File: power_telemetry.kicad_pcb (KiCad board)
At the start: 2 copper layers, 86.5 x 70 mm, 44 parts, among them J1 CONN_01X02, J10 CONN_01X04, J11 CONN_01X04, J12 GS2, J2 Screw_Terminal_1x02, J3 Screw_Terminal_1x02, J4 CONN_01X03, J5 CONN_01X02, J6 CONN_01X03, J7 CONN_01X02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

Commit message: more pcb latyout
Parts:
- moved R14 10.6 mm to (122.5, 94.2), turned to 0 degrees
- moved C8 8.33 mm to (132.9, 87.3)
- moved C2 8.33 mm to (130.3, 87.3)
- moved R10 8.19 mm to (155.8, 89.9)
- moved R11 8.19 mm to (151.1, 91.9)
- moved R13 8.19 mm to (146.2, 89.9)
- moved R5 8.14 mm to (125.2, 100.5)
- moved R12 7.24 mm to (146.2, 82.8)
- moved R9 7.24 mm to (151.0, 80.8)
- moved R8 7.24 mm to (155.7, 82.8)
- moved U2 5.36 mm to (137.9, 86.3), turned to 0 degrees
- moved R4 4.91 mm to (121.9, 100.5)
- moved J12 4.45 mm to (128.0, 94.2), turned to 270 degrees
- moved J1 3.25 mm to (147.4, 100.0)
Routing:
- net /SDA: track 23.5 -> 59.3 mm
- net +12V: track 184.7 -> 153.0 mm
- net Net-(J10-Pad4): track 39.0 -> 17.2 mm
- net /SCL: track 48.3 -> 31.6 mm
- net Net-(J11-Pad4): track 24.0 -> 10.0 mm
- net Net-(R11-Pad1): track 13.9 -> 27.1 mm
- net VCC: track 99.5 -> 90.9 mm
- net Net-(R12-Pad1): track 13.3 -> 18.2 mm
- net Net-(J12-Pad2): track 0.00 -> 2.98 mm
- net GND: track 27.0 -> 25.4 mm, vias 13 -> 12

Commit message: some changes
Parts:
- moved R14 14.7 mm to (136.7, 98.1)
- moved J12 13.7 mm to (141.5, 96.6), turned to 180 degrees
- moved D2 6.68 mm to (154.6, 79.9)
- moved C1 6.40 mm to (112.0, 96.2)
- moved C7 6.40 mm to (112.0, 93.4)
- moved R3 6.40 mm to (97.0, 100.8)
- moved R6 6.40 mm to (105.4, 104.8)
- moved R7 6.40 mm to (105.4, 96.8)
- moved U1 6.40 mm to (116.7, 100.4)
- moved C3 6.40 mm to (108.6, 100.8)
- moved R5 6.33 mm to (129.7, 105.0)
- moved R4 6.33 mm to (126.3, 105.0)
- moved F6 4.80 mm to (83.3, 93.6)
- moved C2 4.75 mm to (130.3, 92.1)
- moved C8 4.75 mm to (132.9, 92.1)
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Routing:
- net Net-(J10-Pad3): track 2.70 -> 38.7 mm
- net Net-(J11-Pad3): track 2.75 -> 34.9 mm
- net VCC: track 90.9 -> 120.0 mm
- net Net-(J10-Pad4): track 17.2 -> 41.2 mm, vias 0 -> 2
- net Net-(J11-Pad4): track 10.0 -> 28.1 mm
- net /SCL: track 31.6 -> 49.3 mm, vias 0 -> 2
- net Net-(F6-Pad1): track 44.9 -> 31.3 mm
- net Net-(J12-Pad2): track 2.98 -> 12.8 mm
- net Net-(F6-Pad2): track 5.86 -> 10.7 mm
- net +12V: track 153.0 -> 157.4 mm
- net /SDA: track 59.3 -> 57.9 mm
- net GND: track 25.4 -> 26.8 mm, vias 12 -> 13
- net (no net): vias 0 -> 1
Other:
- board size 86.5 x 70 mm -> 86.5 x 62 mm

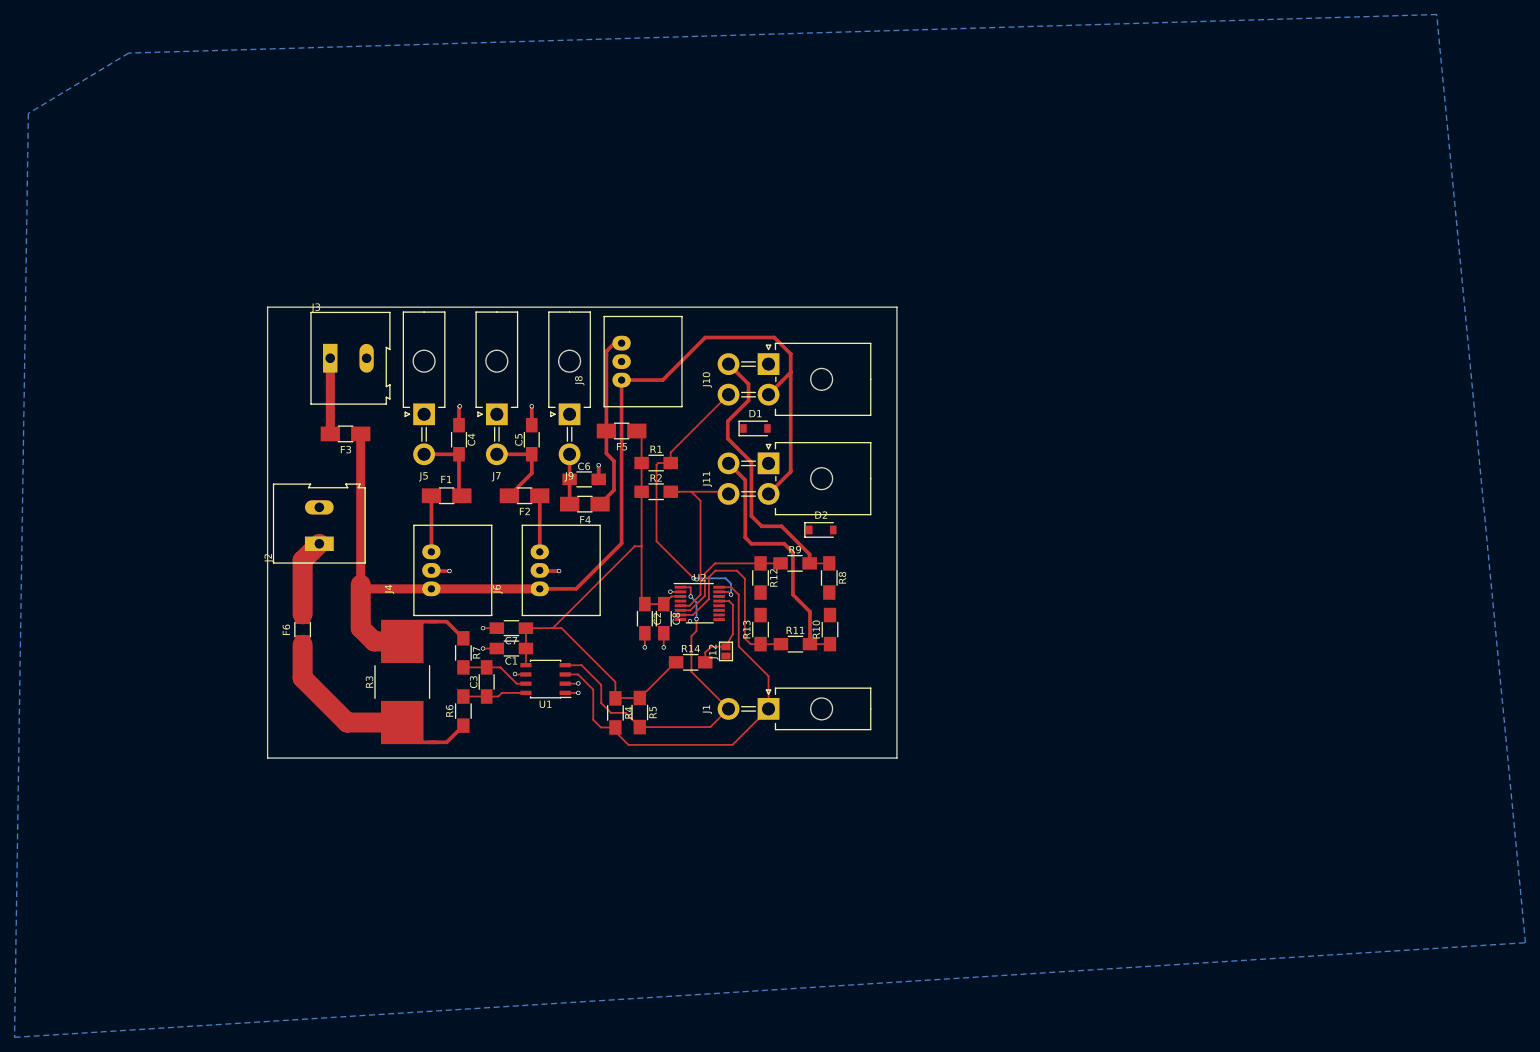
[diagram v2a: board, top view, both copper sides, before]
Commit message: using 5v fan, added graphics
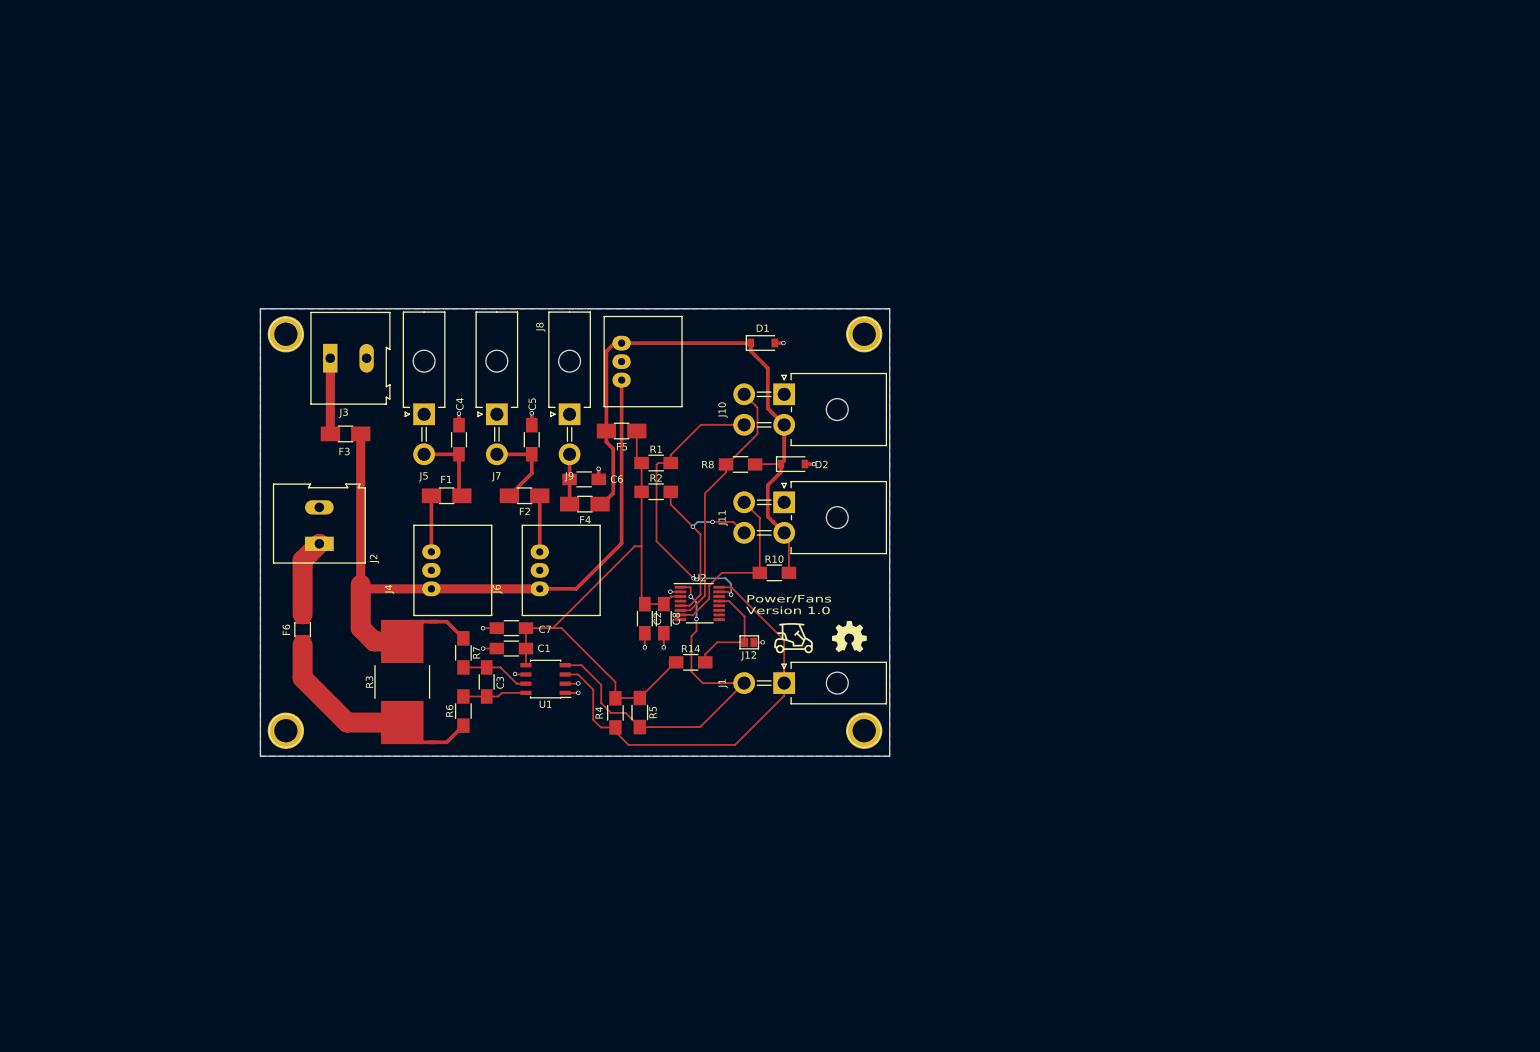
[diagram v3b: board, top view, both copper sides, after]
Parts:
- removed R11, R9: 10k, Resistors_SMD:R_1206_HandSoldering
- removed R12, R13: 4.7k, Resistors_SMD:R_1206_HandSoldering
- added G***: LOGO, lib_fp:golf_cart, F.Cu at (150.8, 94.8)
- added G***: LOGO, lib_fp:OSHW-Logo_2, F.Cu at (158.4, 94.6)
- added REF**: 1pin, Connectors:1pin, F.Cu at (81.0, 107.5)
- added REF**: 1pin, Connectors:1pin, F.Cu at (160.5, 107.5)
- added REF**: 1pin, Connectors:1pin, F.Cu at (160.5, 53.0)
- added REF**: 1pin, Connectors:1pin, F.Cu at (81.0, 53.0)
- moved R8 19.8 mm to (143.5, 70.9), turned to 0 degrees
- moved D1 11.8 mm to (146.6, 54.2)
- moved R10 10.9 mm to (148.2, 85.8), turned to 0 degrees
- moved D2 9.85 mm to (150.7, 70.8)
- moved J11 5.77 mm to (149.5, 76.1)
- moved J10 4.67 mm to (149.5, 61.2)
- moved J1 4.15 mm to (149.5, 101.0)
- moved J12 3.44 mm to (144.7, 95.3), turned to 270 degrees
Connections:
- C4 pad 2: Net-(C4-Pad2) -> VCC
- C5 pad 1: Net-(C5-Pad1) -> VCC
- C6 pad 1: Net-(C6-Pad1) -> VCC
- D1 pad 1: +12V -> VCC
- D2 pad 1: +12V -> VCC
- F1 pad 2: Net-(C4-Pad2) -> VCC
- F2 pad 2: Net-(C5-Pad1) -> VCC
- F4 pad 2: Net-(C6-Pad1) -> VCC
- J10 pad 2: +12V -> VCC
- J11 pad 2: +12V -> VCC
- J5 pad 2: Net-(C4-Pad2) -> VCC
- J7 pad 2: Net-(C5-Pad1) -> VCC
- J9 pad 2: Net-(C6-Pad1) -> VCC
- R10 pad 2: +12V -> VCC
- R8 pad 2: +12V -> VCC
- U2 pad 10: Net-(U2-Pad10) -> (no net)
- U2 pad 11: Net-(U2-Pad11) -> (no net)
- U2 pad 12: Net-(U2-Pad12) -> (no net)
- U2 pad 14: Net-(U2-Pad14) -> (no net)
- U2 pad 4: Net-(U2-Pad4) -> (no net)
- U2 pad 6: Net-(R12-Pad1) -> Net-(J10-Pad3)
- U2 pad 7: Net-(R11-Pad1) -> Net-(J11-Pad3)
- U2 pad 8: Net-(U2-Pad8) -> (no net)
- U2 pad 9: Net-(U2-Pad9) -> (no net)
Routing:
- net VCC: track 120.0 -> 208.4 mm
- net +12V: track 157.4 -> 106.0 mm
- net Net-(R11-Pad1): track 27.1 -> 0.00 mm
- net Net-(R12-Pad1): track 18.2 -> 0.00 mm
- net Net-(C5-Pad1): track 11.8 -> 0.00 mm
- net Net-(C4-Pad2): track 10.7 -> 0.00 mm
- net Net-(J11-Pad3): track 34.9 -> 25.0 mm
- net Net-(C6-Pad1): track 6.85 -> 0.00 mm
- net /SCL: track 49.3 -> 53.6 mm
- net GND: track 26.8 -> 23.0 mm, vias 13 -> 14
- net /SDA: track 57.9 -> 61.0 mm
- net Net-(J10-Pad3): track 38.7 -> 35.7 mm
- net Net-(J12-Pad2): track 12.8 -> 15.3 mm
- net Net-(J11-Pad4): track 28.1 -> 27.9 mm, vias 0 -> 2
- net (no net): vias 1 -> 0
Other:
- board size 86.5 x 62 mm -> 86.5 x 61.5 mm
- board text added: "Power/Fans Version 1.0"

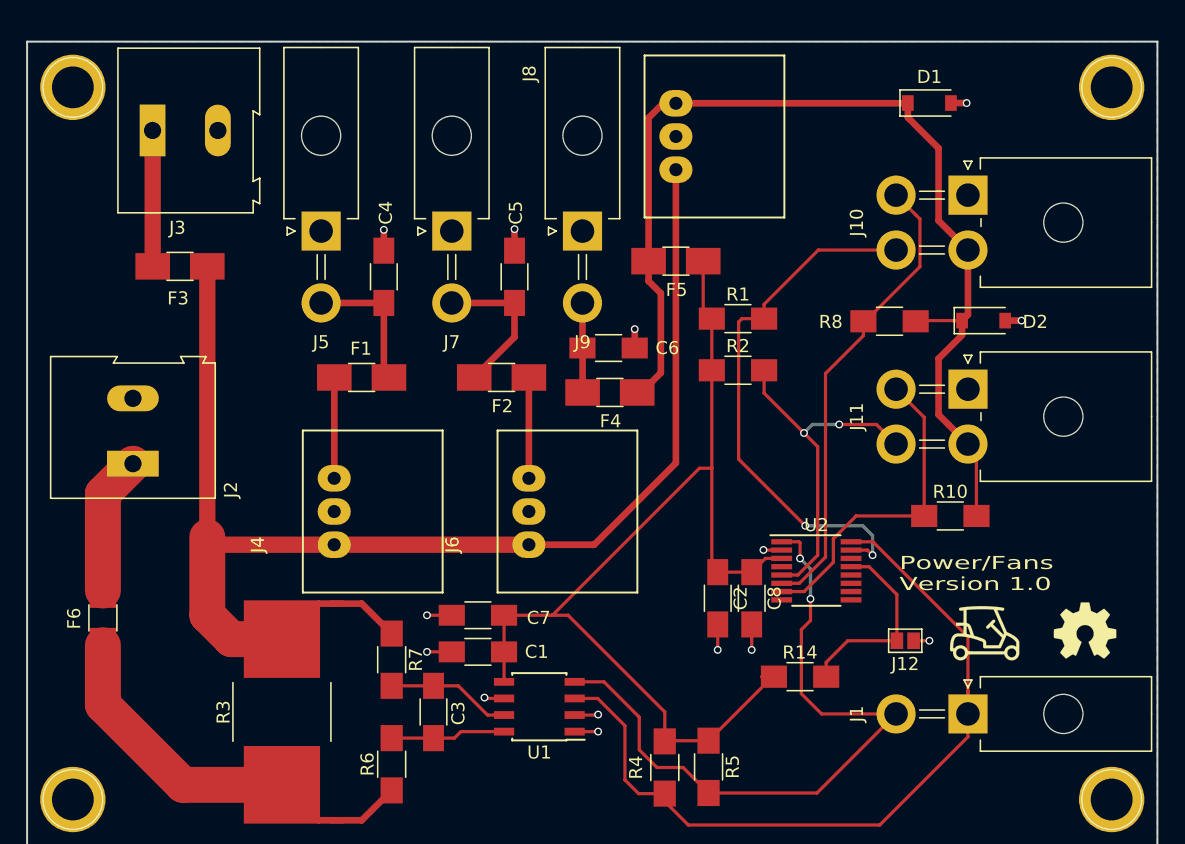
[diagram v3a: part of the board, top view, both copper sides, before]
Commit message: switched power connectors
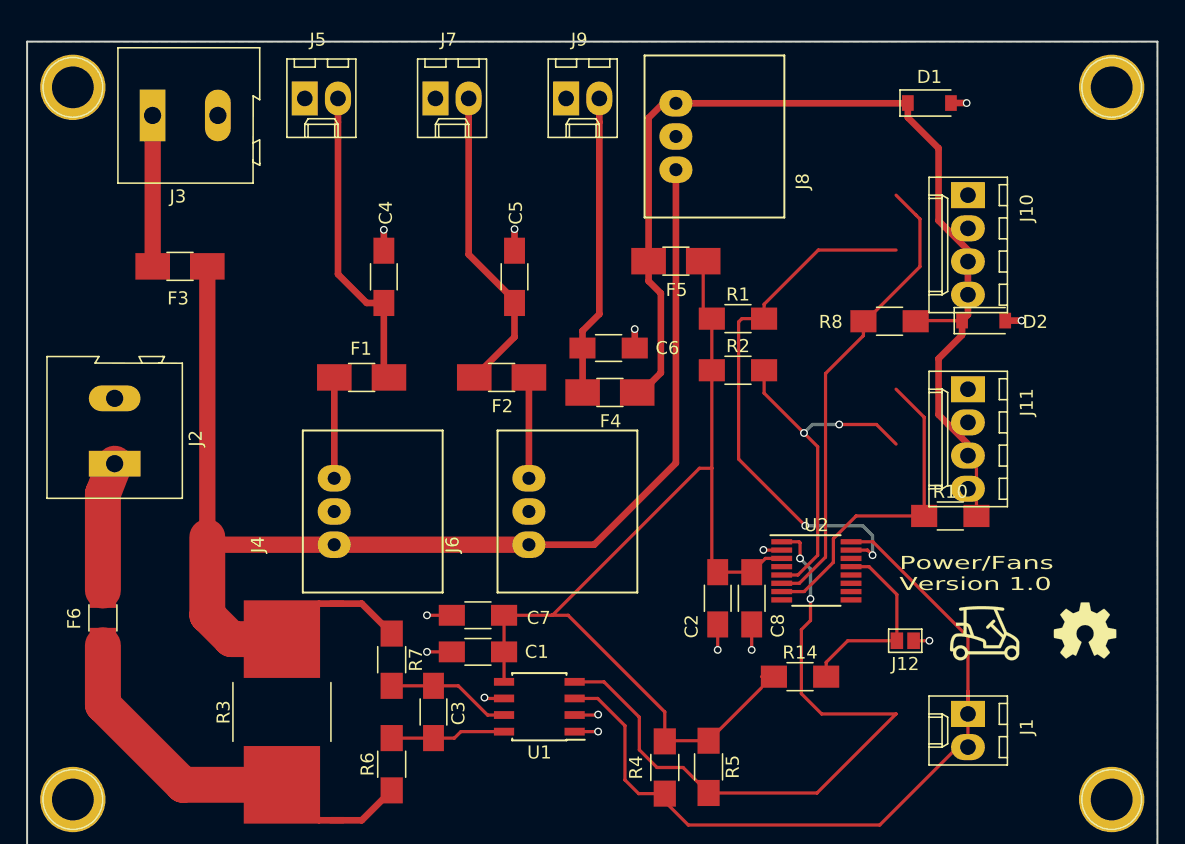
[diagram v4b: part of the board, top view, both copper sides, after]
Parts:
- J1, J5, J7, J9: footprint Connectors_Molex:Molex_MiniFit-JR-5569-02A2_2x01x4.20mm_Angled -> Connectors_Molex:Molex_KK-6410-02_02x2.54mm_Straight
- J10, J11: footprint Connectors_Molex:Molex_MiniFit-JR-5569-04A2_2x02x4.20mm_Angled -> Connectors_Molex:Molex_KK-6410-04_04x2.54mm_Straight
- J2, J3: footprint Connectors:AK300-2 -> lib_fp:TER-202
- moved J5 10.2 mm to (98.8, 53.9)
- moved J7 10.2 mm to (108.8, 53.9)
- moved J9 10.2 mm to (118.8, 53.9)
- moved J2 1.40 mm to (84.2, 81.8)
- moved J3 1.15 mm to (87.1, 55.1)
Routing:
- net VCC: track 208.4 -> 239.9 mm
- net /SDA: track 61.0 -> 36.9 mm
- net /SCL: track 53.6 -> 77.8 mm
- net Net-(J11-Pad3): track 25.0 -> 32.8 mm
- net Net-(J10-Pad3): track 35.7 -> 37.8 mm
- net Net-(F3-Pad2): track 10.4 -> 11.6 mm
- net Net-(F6-Pad2): track 10.7 -> 9.88 mm

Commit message: define some parts and switch to 4 pad shunt resistor
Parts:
- added C10: 10uF, Capacitors_SMD:C_1206_HandSoldering, F.Cu at (115.8, 60.0)
- added C11: 10uF, Capacitors_SMD:C_1206_HandSoldering, F.Cu at (120.0, 63.1)
- added C9: 10uF, Capacitors_SMD:C_1206_HandSoldering, F.Cu at (100.0, 69.0)
- added J13: CONN_01X02, Connectors_Molex:Molex_KK-6410-02_02x2.54mm_Straight, F.Cu at (98.7, 61.4)
- F1, F2, F4: value 1.5A Polyfuse -> 1.0A PTC
- F3: value 5A Polyfuse -> 2.0A PTC
- moved C4 4.97 mm to (100.0, 66.4), turned to 0 degrees
- moved C1 2.80 mm to (112.0, 93.4)
- moved C7 2.75 mm to (112.0, 96.2)
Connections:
- C4 pad 2: VCC -> Net-(C4-Pad2)
- C5 pad 1: VCC -> Net-(C10-Pad2)
- C6 pad 1: VCC -> Net-(C11-Pad2)
- F1 pad 2: VCC -> Net-(C4-Pad2)
- F2 pad 2: VCC -> Net-(C10-Pad2)
- F4 pad 2: VCC -> Net-(C11-Pad2)
- J5 pad 2: VCC -> Net-(C4-Pad2)
- J7 pad 2: VCC -> Net-(C10-Pad2)
- J9 pad 2: VCC -> Net-(C11-Pad2)
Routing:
- net VCC: track 239.9 -> 168.7 mm
- net Net-(C10-Pad2): track 0.00 -> 24.1 mm
- net Net-(C11-Pad2): track 0.00 -> 23.0 mm
- net /SDA: track 36.9 -> 51.5 mm
- net /SCL: track 77.8 -> 63.1 mm
- net GND: track 23.0 -> 21.0 mm, vias 14 -> 13
- net Net-(C4-Pad2): track 0.00 -> 0.55 mm
